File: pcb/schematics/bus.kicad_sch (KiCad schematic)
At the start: 3 parts

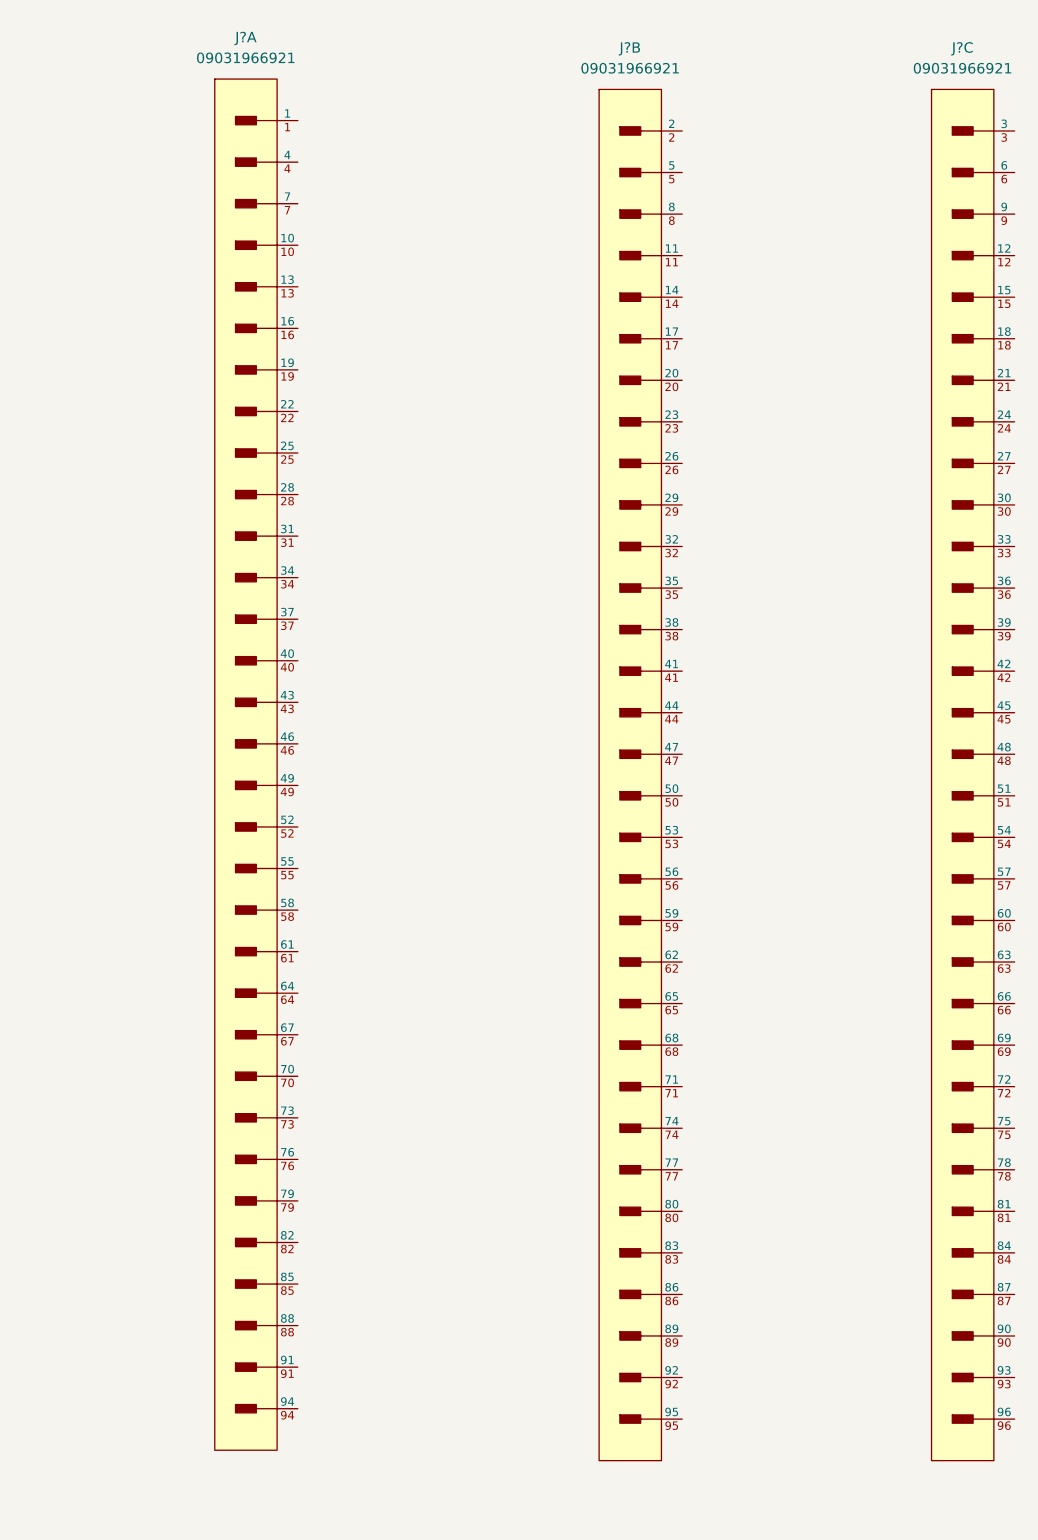
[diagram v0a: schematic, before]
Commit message: add power schematics
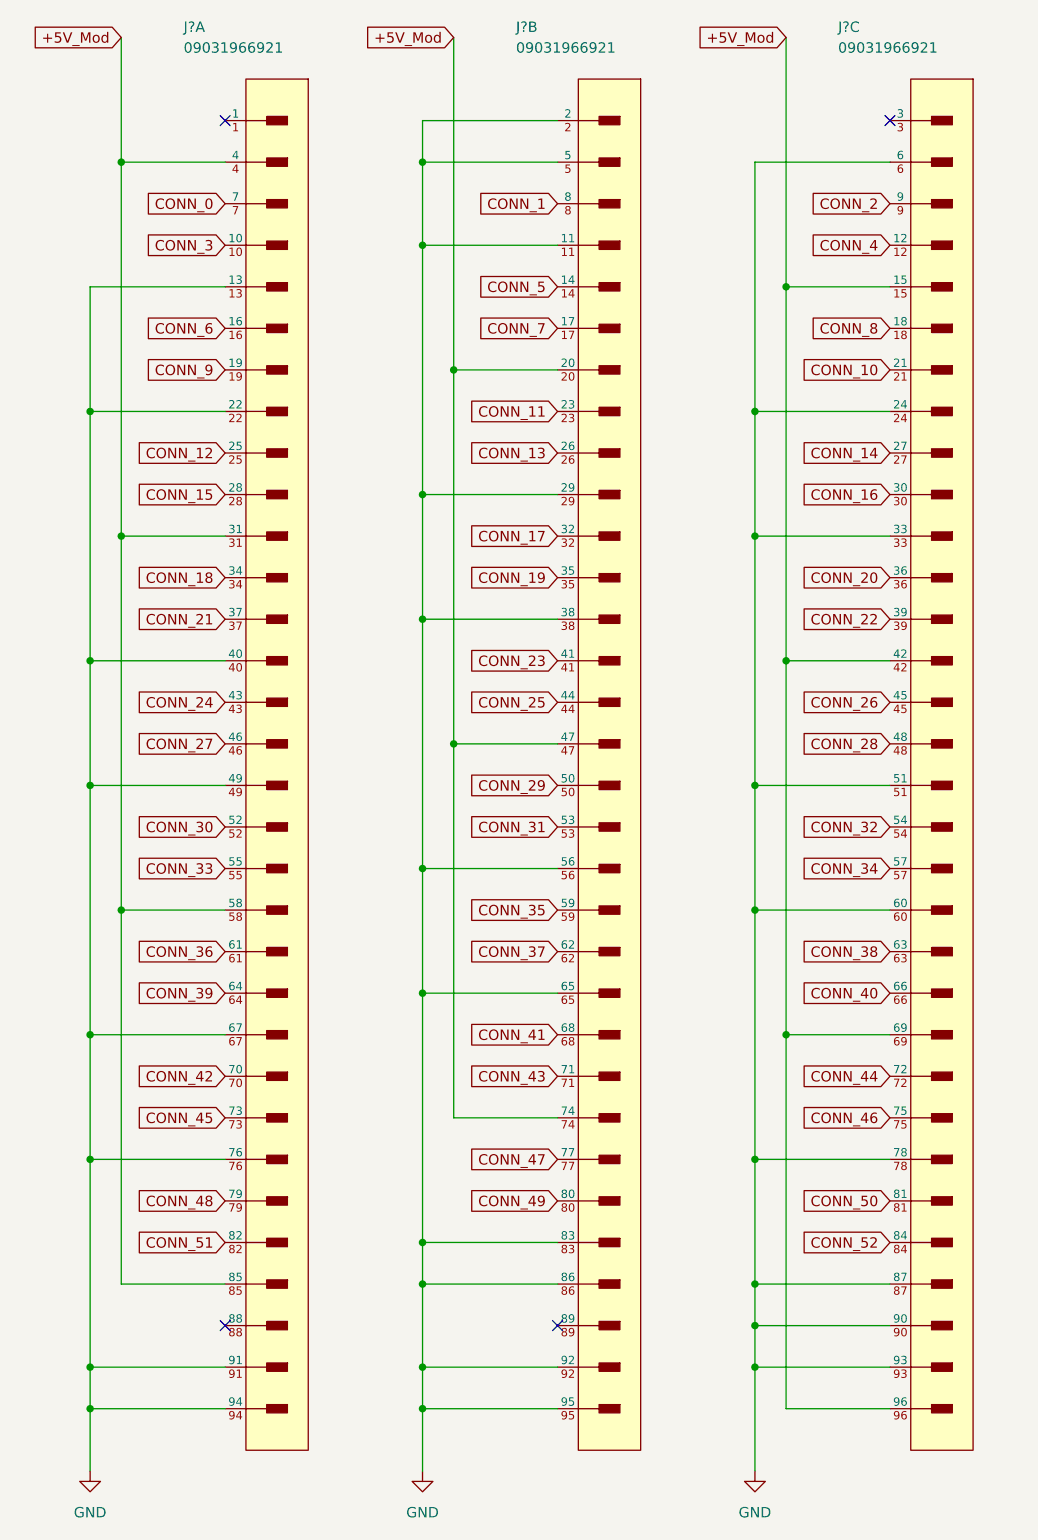
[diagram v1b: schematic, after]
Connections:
- net GND: now reaches J?.11
- net GND: now also J?.13, J?.2, J?.22, J?.24, J?.29, J?.33, J?.38, J?.40, J?.49, J?.5, J?.51, J?.56, J?.6, J?.60, J?.65, J?.67, J?.76, J?.78, J?.83, J?.86, J?.87, J?.90, J?.91, J?.92, J?.93, J?.94, J?.95
- net CONN_5: now reaches J?.14
- net CONN_7: now reaches J?.17
- net +5V_Mod: now reaches J?.20
- net +5V_Mod: now also J?.15, J?.31, J?.4, J?.42, J?.47, J?.58, J?.69, J?.74, J?.85, J?.96
- net CONN_11: now reaches J?.23
- net CONN_13: now reaches J?.26
- net CONN_17: now reaches J?.32
- net CONN_19: now reaches J?.35
- net CONN_23: now reaches J?.41
- net CONN_25: now reaches J?.44
- net CONN_29: now reaches J?.50
- net CONN_31: now reaches J?.53
- net CONN_35: now reaches J?.59
- net CONN_37: now reaches J?.62
- net CONN_41: now reaches J?.68
- net CONN_43: now reaches J?.71
- net CONN_47: now reaches J?.77
- net CONN_1: now reaches J?.8
- net CONN_49: now reaches J?.80
- net CONN_3: now reaches J?.10
- net CONN_6: now reaches J?.16
- net CONN_9: now reaches J?.19
- net CONN_12: now reaches J?.25
- net CONN_15: now reaches J?.28
- net CONN_18: now reaches J?.34
- net CONN_21: now reaches J?.37
- net CONN_24: now reaches J?.43
- net CONN_27: now reaches J?.46
- net CONN_30: now reaches J?.52
- net CONN_33: now reaches J?.55
- net CONN_36: now reaches J?.61
- net CONN_39: now reaches J?.64
- net CONN_0: now reaches J?.7
- net CONN_42: now reaches J?.70
- net CONN_45: now reaches J?.73
- net CONN_48: now reaches J?.79
- net CONN_51: now reaches J?.82
- net CONN_4: now reaches J?.12
- net CONN_8: now reaches J?.18
- net CONN_10: now reaches J?.21
- net CONN_14: now reaches J?.27
- net CONN_16: now reaches J?.30
- net CONN_20: now reaches J?.36
- net CONN_22: now reaches J?.39
- net CONN_26: now reaches J?.45
- net CONN_28: now reaches J?.48
- net CONN_32: now reaches J?.54
- net CONN_34: now reaches J?.57
- net CONN_38: now reaches J?.63
- net CONN_40: now reaches J?.66
- net CONN_44: now reaches J?.72
- net CONN_46: now reaches J?.75
- net CONN_50: now reaches J?.81
- net CONN_52: now reaches J?.84
- net CONN_2: now reaches J?.9
- no-connect marks 0 -> 4
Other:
- moved on the sheet: J?A, J?B, J?C

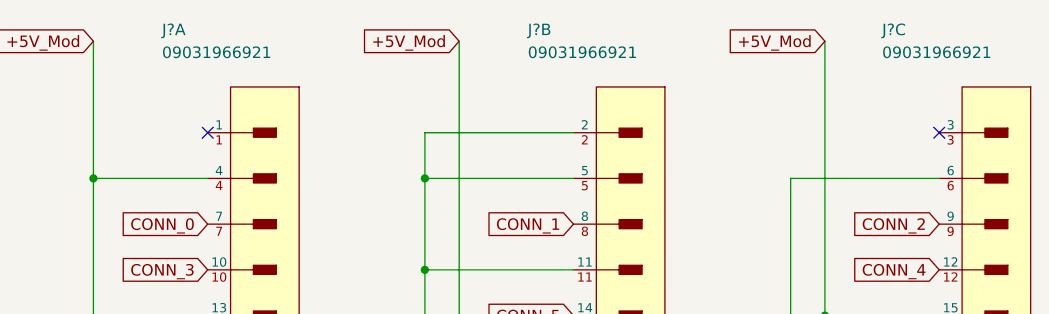
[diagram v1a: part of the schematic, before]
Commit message: start choosing components, need to add overcurren t protection
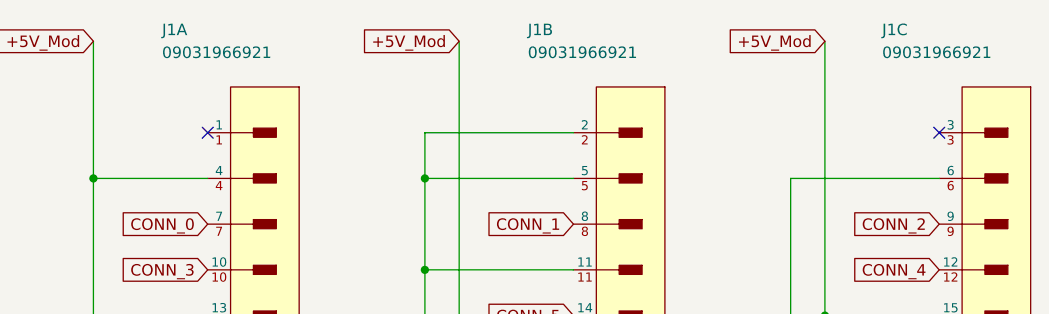
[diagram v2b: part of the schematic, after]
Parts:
- gave numbers to parts that had none: 1
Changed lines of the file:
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@@
   (symbol (lib_id "Conn-09031966821:09031966921") (at 116.84 26.67 0) (mirror y) (unit 2)
     (in_bom yes) (on_board yes)
-    (property "Reference" "J?" (id 0) (at 114.3 15.24 0)
+    (property "Reference" "J1" (id 0) (at 114.3 15.24 0)
       (effects (font (size 1.27 1.27)) (justify right))
     )
@@
   (symbol (lib_id "Conn-09031966821:09031966921") (at 76.2 26.67 0) (mirror y) (unit 1)
     (in_bom yes) (on_board yes)
-    (property "Reference" "J?" (id 0) (at 73.66 15.24 0)
+    (property "Reference" "J1" (id 0) (at 73.66 15.24 0)
       (effects (font (size 1.27 1.27)) (justify right))
     )
@@
   (symbol (lib_id "power:GND") (at 62.23 191.77 0) (unit 1)
     (in_bom yes) (on_board yes) (fields_autoplaced)
-    (property "Reference" "#PWR?" (id 0) (at 62.23 198.12 0)
+    (property "Reference" "#PWR036" (id 0) (at 62.23 198.12 0)
       (effects (font (size 1.27 1.27)) hide)
     )
@@
   (symbol (lib_id "power:GND") (at 102.87 191.77 0) (unit 1)
     (in_bom yes) (on_board yes) (fields_autoplaced)
-    (property "Reference" "#PWR?" (id 0) (at 102.87 198.12 0)
+    (property "Reference" "#PWR037" (id 0) (at 102.87 198.12 0)
       (effects (font (size 1.27 1.27)) hide)
     )
@@
   (symbol (lib_id "Conn-09031966821:09031966921") (at 157.48 26.67 0) (mirror y) (unit 3)
     (in_bom yes) (on_board yes)
-    (property "Reference" "J?" (id 0) (at 153.67 15.24 0)
+    (property "Reference" "J1" (id 0) (at 153.67 15.24 0)
       (effects (font (size 1.27 1.27)) (justify right))
     )
@@
   (symbol (lib_id "power:GND") (at 143.51 191.77 0) (unit 1)
     (in_bom yes) (on_board yes) (fields_autoplaced)
-    (property "Reference" "#PWR?" (id 0) (at 143.51 198.12 0)
-      (effects (font (size 1.27 1.27)) hide)
-    )
+    (property "Reference" "#PWR038" (id 0) (at 143.51 198.12 0)
+      (effects (font (size 1.27 1.27)) hide)
+    )

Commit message: finish the schematic
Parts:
- J1: value 09031966921 -> 09732966801; Part Number (none) -> 09732966801
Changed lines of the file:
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@@
       (effects (font (size 1.27 1.27)) (justify right))
     )
-    (property "Value" "09031966921" (id 1) (at 114.3 17.78 0)
+    (property "Value" "09732966801" (id 1) (at 114.3 17.78 0)
       (effects (font (size 1.27 1.27)) (justify right))
     )
@@
     (property "temperature range low" "-55°C" (id 25) (at 116.84 -44.45 0)
       (effects (font (size 1.27 1.27)) (justify left) hide)
+    )
+    (property "Part Number" "09732966801" (id 26) (at 116.84 26.67 0)
+      (effects (font (size 1.27 1.27)) hide)
     )
     (pin "11")
@@
       (effects (font (size 1.27 1.27)) (justify right))
     )
-    (property "Value" "09031966921" (id 1) (at 73.66 17.78 0)
+    (property "Value" "09732966801" (id 1) (at 73.66 17.78 0)
       (effects (font (size 1.27 1.27)) (justify right))
     )
@@
     (property "temperature range low" "-55°C" (id 25) (at 76.2 -44.45 0)
       (effects (font (size 1.27 1.27)) (justify left) hide)
+    )
+    (property "Part Number" "09732966801" (id 26) (at 76.2 26.67 0)
+      (effects (font (size 1.27 1.27)) hide)
     )
     (pin "1")
@@
       (effects (font (size 1.27 1.27)) (justify right))
     )
-    (property "Value" "09031966921" (id 1) (at 153.67 17.78 0)
+    (property "Value" "09732966801" (id 1) (at 153.67 17.78 0)
       (effects (font (size 1.27 1.27)) (justify right))
     )
@@
       (effects (font (size 1.27 1.27)) (justify left) hide)
     )
+    (property "Part Number" "09732966801" (id 26) (at 157.48 26.67 0)
+      (effects (font (size 1.27 1.27)) hide)
+    )
     (pin "12")

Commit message: add components to the pcb
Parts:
- J1: footprint Harting-09031966921-0-0-* -> 09031966821:Harting-09031966921-0-0-0
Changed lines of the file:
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@@
       (effects (font (size 1.27 1.27)) (justify right))
     )
-    (property "Footprint" "Harting-09031966921-0-0-*" (id 2) (at 116.84 13.97 0)
+    (property "Footprint" "09031966821:Harting-09031966921-0-0-0" (id 2) (at 116.84 13.97 0)
       (effects (font (size 1.27 1.27)) (justify left) hide)
     )
@@
       (effects (font (size 1.27 1.27)) (justify right))
     )
-    (property "Footprint" "Harting-09031966921-0-0-*" (id 2) (at 76.2 13.97 0)
+    (property "Footprint" "09031966821:Harting-09031966921-0-0-0" (id 2) (at 76.2 13.97 0)
       (effects (font (size 1.27 1.27)) (justify left) hide)
     )
@@
       (effects (font (size 1.27 1.27)) (justify right))
     )
-    (property "Footprint" "Harting-09031966921-0-0-*" (id 2) (at 157.48 13.97 0)
-      (effects (font (size 1.27 1.27)) (justify left) hide)
-    )
+    (property "Footprint" "09031966821:Harting-09031966921-0-0-0" (id 2) (at 157.48 13.97 0)
+      (effects (font (size 1.27 1.27)) (justify left) hide)
+    )

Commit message: start placing components
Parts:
- J1: value 09732966801 -> 09032967825; footprint 09031966821:Harting-09031966921-0-0-0 -> 09031966821:09032967825; Part Number 09732966801 -> 09032967825
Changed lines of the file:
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@@
       (effects (font (size 1.27 1.27)) (justify right))
     )
-    (property "Value" "09732966801" (id 1) (at 114.3 17.78 0)
-      (effects (font (size 1.27 1.27)) (justify right))
-    )
-    (property "Footprint" "09031966821:Harting-09031966921-0-0-0" (id 2) (at 116.84 13.97 0)
+    (property "Value" "09032967825" (id 1) (at 114.3 17.78 0)
+      (effects (font (size 1.27 1.27)) (justify right))
+    )
+    (property "Footprint" "09031966821:09032967825" (id 2) (at 116.84 13.97 0)
       (effects (font (size 1.27 1.27)) (justify left) hide)
     )
@@
       (effects (font (size 1.27 1.27)) (justify left) hide)
     )
-    (property "Part Number" "09732966801" (id 26) (at 116.84 26.67 0)
+    (property "Part Number" "09032967825" (id 26) (at 116.84 26.67 0)
       (effects (font (size 1.27 1.27)) hide)
     )
@@
       (effects (font (size 1.27 1.27)) (justify right))
     )
-    (property "Value" "09732966801" (id 1) (at 73.66 17.78 0)
-      (effects (font (size 1.27 1.27)) (justify right))
-    )
-    (property "Footprint" "09031966821:Harting-09031966921-0-0-0" (id 2) (at 76.2 13.97 0)
+    (property "Value" "09032967825" (id 1) (at 73.66 17.78 0)
+      (effects (font (size 1.27 1.27)) (justify right))
+    )
+    (property "Footprint" "09031966821:09032967825" (id 2) (at 76.2 13.97 0)
       (effects (font (size 1.27 1.27)) (justify left) hide)
     )
@@
       (effects (font (size 1.27 1.27)) (justify left) hide)
     )
-    (property "Part Number" "09732966801" (id 26) (at 76.2 26.67 0)
+    (property "Part Number" "09032967825" (id 26) (at 76.2 26.67 0)
       (effects (font (size 1.27 1.27)) hide)
     )
@@
       (effects (font (size 1.27 1.27)) (justify right))
     )
-    (property "Value" "09732966801" (id 1) (at 153.67 17.78 0)
-      (effects (font (size 1.27 1.27)) (justify right))
-    )
-    (property "Footprint" "09031966821:Harting-09031966921-0-0-0" (id 2) (at 157.48 13.97 0)
+    (property "Value" "09032967825" (id 1) (at 153.67 17.78 0)
+      (effects (font (size 1.27 1.27)) (justify right))
+    )
+    (property "Footprint" "09031966821:09032967825" (id 2) (at 157.48 13.97 0)
       (effects (font (size 1.27 1.27)) (justify left) hide)
     )
@@
       (effects (font (size 1.27 1.27)) (justify left) hide)
     )
-    (property "Part Number" "09732966801" (id 26) (at 157.48 26.67 0)
-      (effects (font (size 1.27 1.27)) hide)
-    )
+    (property "Part Number" "09032967825" (id 26) (at 157.48 26.67 0)
+      (effects (font (size 1.27 1.27)) hide)
+    )

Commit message: route more components
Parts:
- J1: footprint 09031966821:09032967825 -> 09031966821:Harting-09031966921-0-0-0
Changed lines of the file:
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@@
       (effects (font (size 1.27 1.27)) (justify right))
     )
-    (property "Footprint" "09031966821:09032967825" (id 2) (at 116.84 13.97 0)
+    (property "Footprint" "09031966821:Harting-09031966921-0-0-0" (id 2) (at 116.84 13.97 0)
       (effects (font (size 1.27 1.27)) (justify left) hide)
     )
@@
       (effects (font (size 1.27 1.27)) (justify right))
     )
-    (property "Footprint" "09031966821:09032967825" (id 2) (at 76.2 13.97 0)
+    (property "Footprint" "09031966821:Harting-09031966921-0-0-0" (id 2) (at 76.2 13.97 0)
       (effects (font (size 1.27 1.27)) (justify left) hide)
     )
@@
       (effects (font (size 1.27 1.27)) (justify right))
     )
-    (property "Footprint" "09031966821:09032967825" (id 2) (at 157.48 13.97 0)
-      (effects (font (size 1.27 1.27)) (justify left) hide)
-    )
+    (property "Footprint" "09031966821:Harting-09031966921-0-0-0" (id 2) (at 157.48 13.97 0)
+      (effects (font (size 1.27 1.27)) (justify left) hide)
+    )
